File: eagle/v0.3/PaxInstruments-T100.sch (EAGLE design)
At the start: 29 parts, among them U1 Attiny85

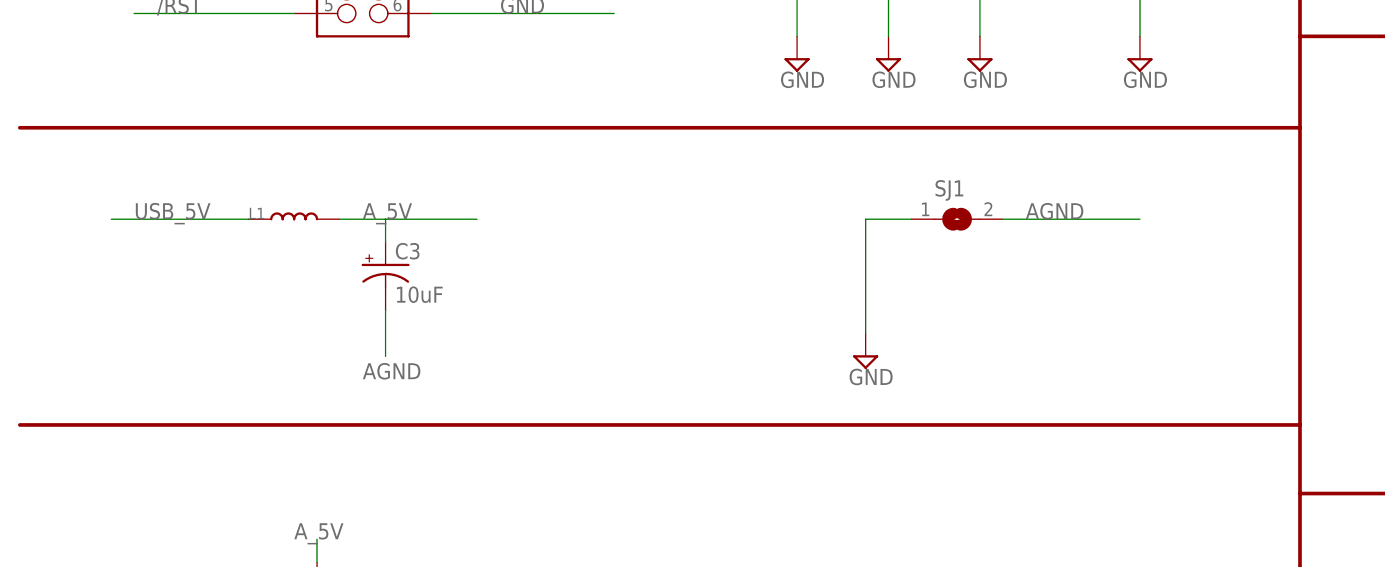
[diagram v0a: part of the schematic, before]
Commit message: Added indicator LED and breakout header.
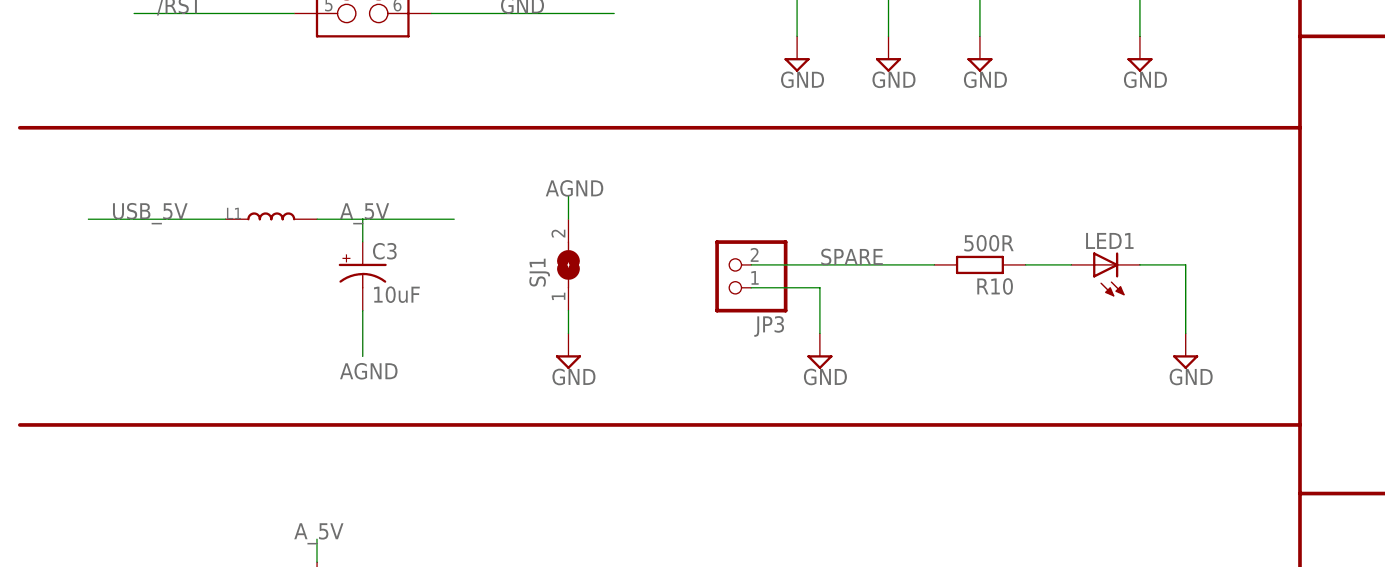
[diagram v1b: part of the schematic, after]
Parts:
- added JP3: (no value), microbuilder:HEADER-1X2ROUND
- added LED1: (no value), SparkFun-LED:LED0603
- added R10: 500R, rcl:R-EU_R0603
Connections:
- new net N$5: LED1.A, R10.1
- net GND: now also JP3.1, LED1.C
- net SPARE: now also JP3.2, R10.2
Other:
- moved on the sheet: C3, L1, SJ1
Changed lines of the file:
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@@
 <part name="U$2" library="PaxInstrument-T400" deviceset="CHARLESPAX_TC-MINI-CONNECTOR" device=""/>
 <part name="SJ1" library="jumper" deviceset="SJ" device=""/>
+<part name="LED1" library="SparkFun-LED" deviceset="LED" device="0603"/>
+<part name="R10" library="rcl" deviceset="R-EU_" device="R0603" value="500R"/>
+<part name="SUPPLY6" library="supply2" deviceset="GND" device=""/>
+<part name="JP3" library="microbuilder" deviceset="HEADER-1X2" device="ROUND"/>
+<part name="SUPPLY8" library="supply2" deviceset="GND" device=""/>
 </parts>
 <sheets>
@@
 <instance part="U$3" gate="G$1" x="203.2" y="144.78"/>
 <instance part="U$4" gate="G$1" x="198.12" y="91.44"/>
-<instance part="L1" gate="L" x="35.56" y="96.52"/>
-<instance part="C3" gate="G$1" x="45.72" y="91.44"/>
-<instance part="SUPPLY7" gate="GND" x="99.06" y="81.28"/>
+<instance part="L1" gate="L" x="33.02" y="96.52"/>
+<instance part="C3" gate="G$1" x="43.18" y="91.44"/>
+<instance part="SUPPLY7" gate="GND" x="66.04" y="81.28"/>
 <instance part="C4" gate="G$1" x="162.56" y="147.32"/>
 <instance part="C5" gate="G$1" x="172.72" y="93.98"/>
@@
 <instance part="R9" gate="G$1" x="106.68" y="157.48" rot="R90"/>
 <instance part="U$2" gate="G$1" x="22.86" y="43.18"/>
-<instance part="SJ1" gate="1" x="109.22" y="96.52"/>
+<instance part="SJ1" gate="1" x="66.04" y="91.44" rot="R90"/>
+<instance part="LED1" gate="G$1" x="124.46" y="91.44" rot="R90"/>
+<instance part="R10" gate="G$1" x="111.76" y="91.44" rot="R180"/>
+<instance part="SUPPLY6" gate="GND" x="134.62" y="81.28"/>
+<instance part="JP3" gate="G$1" x="83.82" y="91.44" rot="R180"/>
+<instance part="SUPPLY8" gate="GND" x="93.98" y="81.28"/>
 </instances>
 <busses>
@@
 <segment>
 <pinref part="L1" gate="L" pin="1"/>
-<wire x1="30.48" y1="96.52" x2="15.24" y2="96.52" width="0.1524" layer="91"/>
-<label x="17.78" y="96.52" size="1.778" layer="95"/>
+<wire x1="27.94" y1="96.52" x2="12.7" y2="96.52" width="0.1524" layer="91"/>
+<label x="15.24" y="96.52" size="1.778" layer="95"/>
 </segment>
 <segment>
@@
 <segment>
 <pinref part="SUPPLY7" gate="GND" pin="GND"/>
-<wire x1="99.06" y1="83.82" x2="99.06" y2="96.52" width="0.1524" layer="91"/>
-<wire x1="99.06" y1="96.52" x2="104.14" y2="96.52" width="0.1524" layer="91"/>
+<wire x1="66.04" y1="83.82" x2="66.04" y2="86.36" width="0.1524" layer="91"/>
 <pinref part="SJ1" gate="1" pin="1"/>
+</segment>
+<segment>
+<pinref part="LED1" gate="G$1" pin="C"/>
+<pinref part="SUPPLY6" gate="GND" pin="GND"/>
+<wire x1="129.54" y1="91.44" x2="134.62" y2="91.44" width="0.1524" layer="91"/>
+<wire x1="134.62" y1="91.44" x2="134.62" y2="83.82" width="0.1524" layer="91"/>
+</segment>
+<segment>
+<pinref part="JP3" gate="G$1" pin="1"/>
+<wire x1="86.36" y1="88.9" x2="93.98" y2="88.9" width="0.1524" layer="91"/>
+<wire x1="93.98" y1="88.9" x2="93.98" y2="83.82" width="0.1524" layer="91"/>
+<pinref part="SUPPLY8" gate="GND" pin="GND"/>
 </segment>
 </net>
@@
 <label x="20.32" y="124.46" size="1.778" layer="95"/>
 <pinref part="JP2" gate="G$1" pin="1"/>
+</segment>
+<segment>
+<pinref part="R10" gate="G$1" pin="2"/>
+<wire x1="106.68" y1="91.44" x2="86.36" y2="91.44" width="0.1524" layer="91"/>
+<label x="93.98" y="91.44" size="1.778" layer="95"/>
+<pinref part="JP3" gate="G$1" pin="2"/>
 </segment>
 </net>
@@
 <pinref part="L1" gate="L" pin="2"/>
 <pinref part="C3" gate="G$1" pin="+"/>
-<wire x1="40.64" y1="96.52" x2="45.72" y2="96.52" width="0.1524" layer="91"/>
-<wire x1="45.72" y1="96.52" x2="45.72" y2="93.98" width="0.1524" layer="91"/>
-<wire x1="45.72" y1="96.52" x2="55.88" y2="96.52" width="0.1524" layer="91"/>
-<label x="43.18" y="96.52" size="1.778" layer="95"/>
+<wire x1="38.1" y1="96.52" x2="43.18" y2="96.52" width="0.1524" layer="91"/>
+<wire x1="43.18" y1="96.52" x2="43.18" y2="93.98" width="0.1524" layer="91"/>
+<wire x1="43.18" y1="96.52" x2="53.34" y2="96.52" width="0.1524" layer="91"/>
+<label x="40.64" y="96.52" size="1.778" layer="95"/>
 </segment>
 <segment>
@@
 <net name="AGND" class="0">
 <segment>
-<wire x1="114.3" y1="96.52" x2="129.54" y2="96.52" width="0.1524" layer="91"/>
-<label x="116.84" y="96.52" size="1.778" layer="95"/>
+<wire x1="66.04" y1="96.52" x2="66.04" y2="99.06" width="0.1524" layer="91"/>
+<label x="63.5" y="99.06" size="1.778" layer="95"/>
 <pinref part="SJ1" gate="1" pin="2"/>
 </segment>
@@
 <segment>
 <pinref part="C3" gate="G$1" pin="-"/>
-<wire x1="45.72" y1="81.28" x2="45.72" y2="86.36" width="0.1524" layer="91"/>
-<label x="43.18" y="78.74" size="1.778" layer="95"/>
+<wire x1="43.18" y1="81.28" x2="43.18" y2="86.36" width="0.1524" layer="91"/>
+<label x="40.64" y="78.74" size="1.778" layer="95"/>
 </segment>
 <segment>
@@
 </segment>
 </net>
+<net name="N$5" class="0">
+<segment>
+<pinref part="R10" gate="G$1" pin="1"/>
+<pinref part="LED1" gate="G$1" pin="A"/>
+<wire x1="121.92" y1="91.44" x2="116.84" y2="91.44" width="0.1524" layer="91"/>
+</segment>
+</net>

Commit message: [V0.3] - initial layout
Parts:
- removed LOGO1: OSHW-LOGOS, SparkFun-Aesthetics:OSHW-LOGOS
- removed SJ1: (no value), jumper:SJ
- removed U$1: PAX-LOGO, charlespax:PAX-LOGO
- removed U$2: CHARLESPAX_TC-MINI-CONNECTOR, PaxInstrument-T400:CHARLESPAX_TC-MINI-CONNECTOR
- added L2: (no value), SeeesStudio-OPL:L-0603
- added U$5: TC-MINI-INSIDE, PaxInstruments-Connectors:TC-MINI-INSIDE
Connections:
- net AGND: now also L2.2; no longer SJ1.2
- net GND: now also L2.1; no longer SJ1.1
- net N$3: now also U$5.P$2; no longer U$2.P$2
- net N$4: now also U$5.P$1; no longer U$2.P$1
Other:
- note added: "v0.3"
- note removed: "v0.2"
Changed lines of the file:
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@@
 <?xml version="1.0" encoding="utf-8"?>
 <!DOCTYPE eagle SYSTEM "eagle.dtd">
-<eagle version="7.0.0">
+<eagle version="7.3.0">
 <drawing>
 <settings>
@@
 <layer number="97" name="Info" color="7" fill="1" visible="yes" active="yes"/>
 <layer number="98" name="Guide" color="6" fill="1" visible="yes" active="yes"/>
+<layer number="99" name="SpiceOrder" color="5" fill="1" visible="yes" active="yes"/>
 <layer number="100" name="Muster" color="7" fill="1" visible="no" active="no"/>
 <layer number="101" name="Patch_Top" color="12" fill="4" visible="no" active="yes"/>
@@
 <part name="C2" library="SparkFun-Capacitors" deviceset="10UF-TANT" device="" value="10uF"/>
 <part name="SUPPLY5" library="supply2" deviceset="GND" device=""/>
-<part name="LOGO1" library="SparkFun-Aesthetics" deviceset="OSHW-LOGO" device="S" value="OSHW-LOGOS"/>
-<part name="U$1" library="charlespax" deviceset="PAX-LOGO" device=""/>
 <part name="U$3" library="SparkFun-DigitalIC" deviceset="MCP3421" device=""/>
 <part name="U$4" library="SparkFun-DigitalIC" deviceset="MCP9800" device=""/>
@@
 <part name="JP2" library="SparkFun-Connectors" deviceset="M03X2" device="SMT"/>
 <part name="R9" library="rcl" deviceset="R-EU_" device="R0603" value="1.2K"/>
-<part name="U$2" library="PaxInstrument-T400" deviceset="CHARLESPAX_TC-MINI-CONNECTOR" device=""/>
-<part name="SJ1" library="jumper" deviceset="SJ" device=""/>
 <part name="LED1" library="SparkFun-LED" deviceset="LED" device="0603"/>
 <part name="R10" library="rcl" deviceset="R-EU_" device="R0603" value="500R"/>
@@
 <part name="JP3" library="microbuilder" deviceset="HEADER-1X2" device="ROUND"/>
 <part name="SUPPLY8" library="supply2" deviceset="GND" device=""/>
+<part name="U$5" library="PaxInstruments-Connectors" deviceset="TC-MINI-INSIDE" device=""/>
+<part name="L2" library="SeeesStudio-OPL" deviceset="L*" device="-0603"/>
 </parts>
 <sheets>
@@
 <wire x1="254" y1="116.84" x2="147.32" y2="116.84" width="0.4064" layer="94"/>
 <wire x1="254" y1="66.04" x2="147.32" y2="66.04" width="0.4064" layer="94"/>
-<text x="248.92" y="5.08" size="2.54" layer="94">v0.2</text>
+<text x="248.92" y="5.08" size="2.54" layer="94">v0.3</text>
 </plain>
 <instances>
@@
 <instance part="C2" gate="G$1" x="129.54" y="129.54"/>
 <instance part="SUPPLY5" gate="GND" x="129.54" y="114.3"/>
-<instance part="LOGO1" gate="G$1" x="175.26" y="15.24"/>
-<instance part="U$1" gate="G$1" x="193.04" y="12.7"/>
 <instance part="U$3" gate="G$1" x="203.2" y="144.78"/>
 <instance part="U$4" gate="G$1" x="198.12" y="91.44"/>
@@
 <instance part="JP2" gate="G$1" x="43.18" y="121.92"/>
 <instance part="R9" gate="G$1" x="106.68" y="157.48" rot="R90"/>
-<instance part="U$2" gate="G$1" x="22.86" y="43.18"/>
-<instance part="SJ1" gate="1" x="66.04" y="91.44" rot="R90"/>
 <instance part="LED1" gate="G$1" x="124.46" y="91.44" rot="R90"/>
 <instance part="R10" gate="G$1" x="111.76" y="91.44" rot="R180"/>
@@
 <instance part="JP3" gate="G$1" x="83.82" y="91.44" rot="R180"/>
 <instance part="SUPPLY8" gate="GND" x="93.98" y="81.28"/>
+<instance part="U$5" gate="G$1" x="22.86" y="43.18"/>
+<instance part="L2" gate="L" x="66.04" y="91.44" rot="R90"/>
 </instances>
 <busses>
@@
 <pinref part="SUPPLY7" gate="GND" pin="GND"/>
 <wire x1="66.04" y1="83.82" x2="66.04" y2="86.36" width="0.1524" layer="91"/>
-<pinref part="SJ1" gate="1" pin="1"/>
+<pinref part="L2" gate="L" pin="1"/>
 </segment>
 <segment>
@@
 <wire x1="66.04" y1="96.52" x2="66.04" y2="99.06" width="0.1524" layer="91"/>
 <label x="63.5" y="99.06" size="1.778" layer="95"/>
-<pinref part="SJ1" gate="1" pin="2"/>
+<pinref part="L2" gate="L" pin="2"/>
 </segment>
 <segment>
@@
 <wire x1="38.1" y1="35.56" x2="38.1" y2="38.1" width="0.1524" layer="91"/>
 <junction x="38.1" y="38.1"/>
-<pinref part="U$2" gate="G$1" pin="P$2"/>
+<pinref part="U$5" gate="G$1" pin="P$2"/>
 </segment>
 </net>
@@
 <wire x1="38.1" y1="48.26" x2="38.1" y2="45.72" width="0.1524" layer="91"/>
 <junction x="38.1" y="45.72"/>
-<pinref part="U$2" gate="G$1" pin="P$1"/>
-</segment>
-</net>
+<pinref part="U$5" gate="G$1" pin="P$1"/>
+</segment>
+</net>
